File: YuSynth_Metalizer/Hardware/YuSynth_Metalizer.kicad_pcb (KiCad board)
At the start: 2 copper layers, 29 x 108 mm, 83 parts, among them J37 CV1, J38 CV2, J39 In, J40 Out, Q1 BC547, Q10 BC547, Q11 BC557, Q12 BC547, Q2 BC547, Q3 BC547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

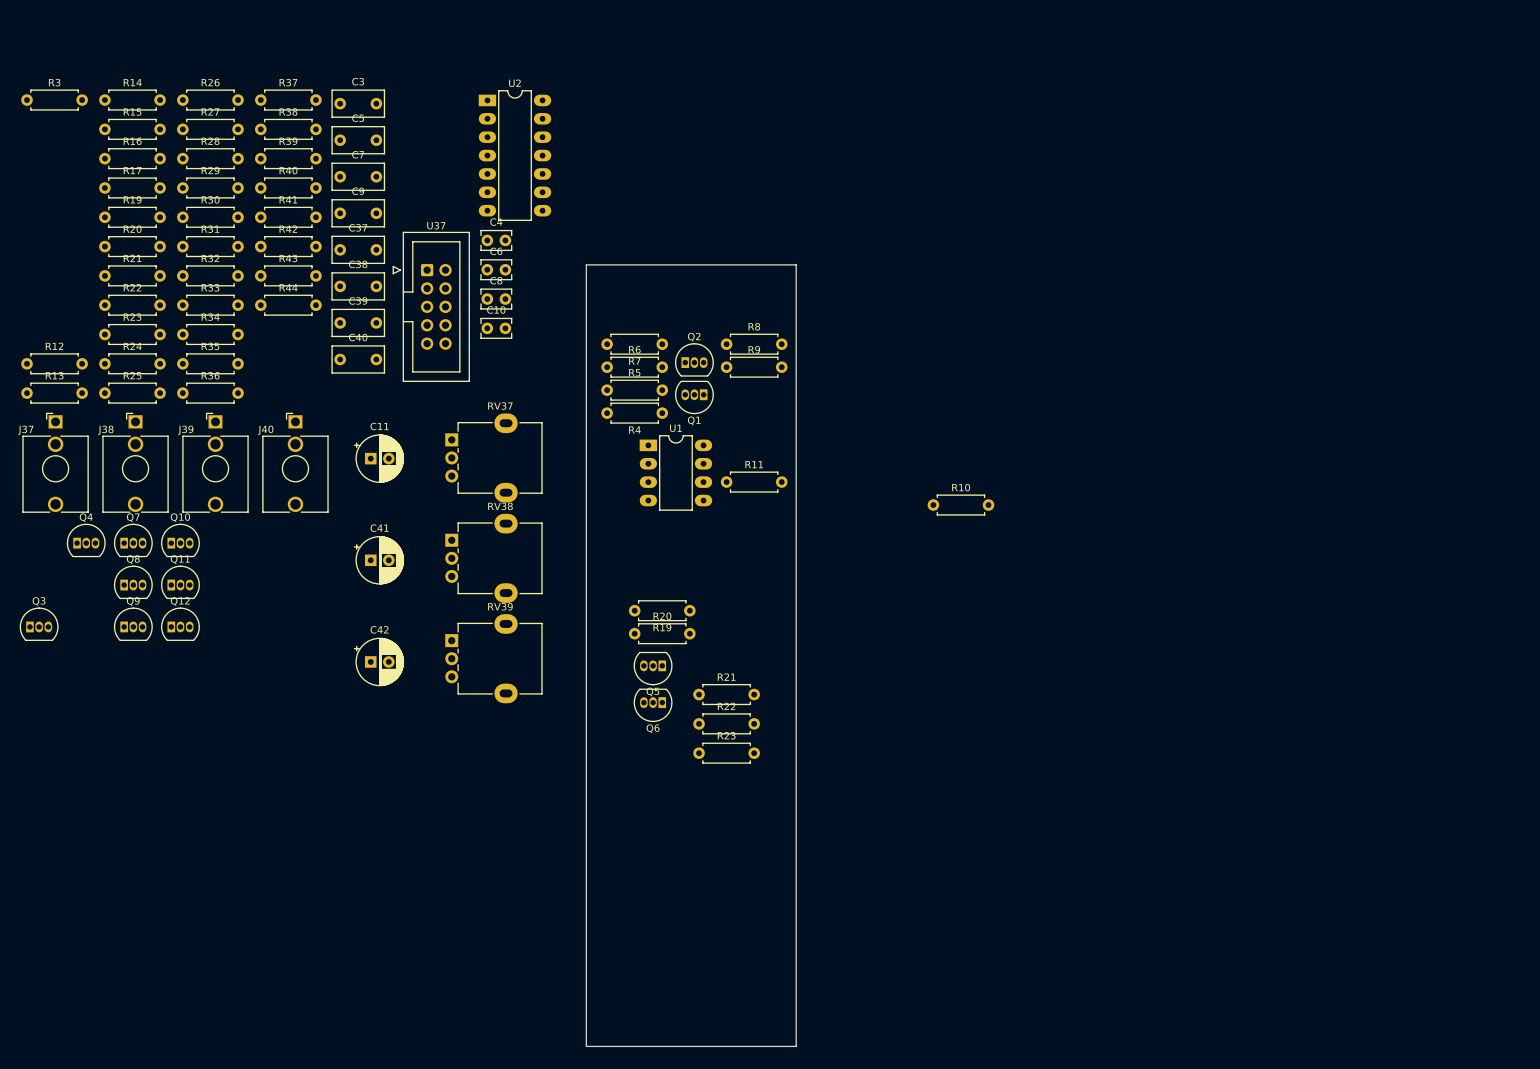
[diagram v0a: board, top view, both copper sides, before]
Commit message: Fixed OpAmp supply range error & redid PCB
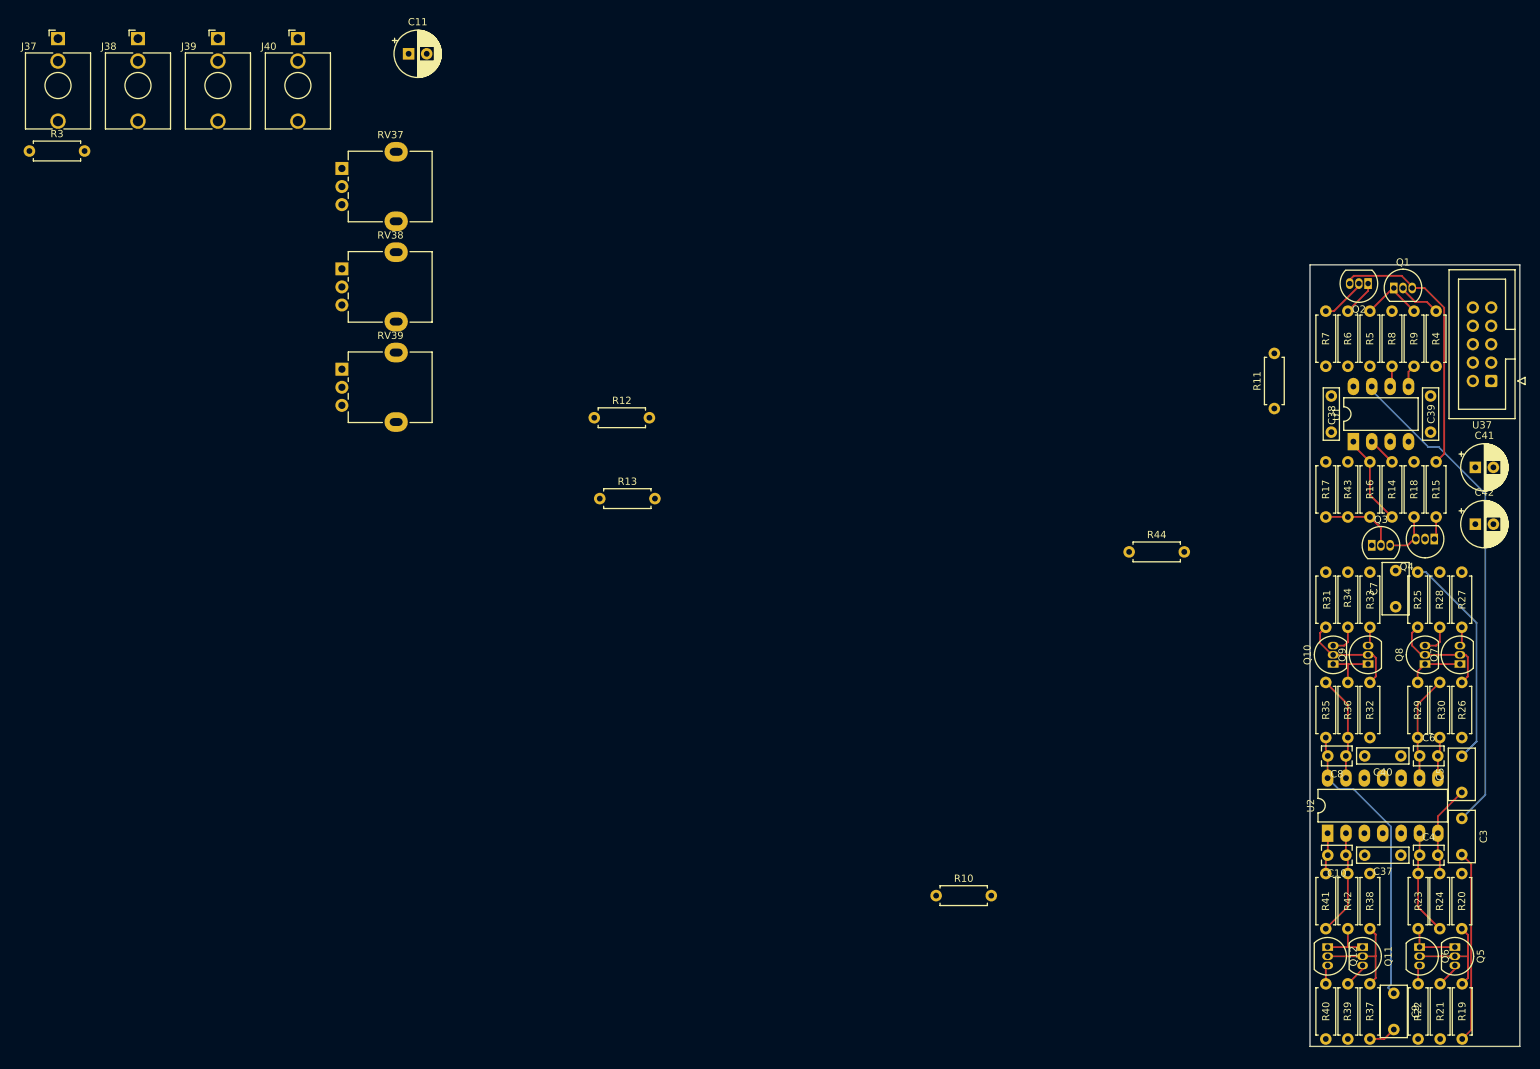
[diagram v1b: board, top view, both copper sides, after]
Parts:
- removed the R19 at (33.5, 43.4)
- removed the R19 at (114.3, 97.8)
- removed the R20 at (33.5, 47.5)
- removed the R20 at (106.7, 101.0)
- removed the R21 at (33.5, 51.5)
- removed the R21 at (115.6, 109.4)
- removed the R22 at (33.5, 55.6)
- removed the R22 at (115.6, 113.4)
- removed the R23 at (115.6, 117.5)
- removed the R23 at (33.5, 59.6)
- added R18: 18k, Resistor_THT:R_Axial_DIN0207_L6.3mm_D2.5mm_P7.62mm_Horizontal, F.Cu at (214.4, 84.8)
- added R19: 27k, Resistor_THT:R_Axial_DIN0207_L6.3mm_D2.5mm_P7.62mm_Horizontal, F.Cu at (221.0, 157.0)
- added R20: 68k, Resistor_THT:R_Axial_DIN0207_L6.3mm_D2.5mm_P7.62mm_Horizontal, F.Cu at (221.0, 141.7)
- added R21: 22k, Resistor_THT:R_Axial_DIN0207_L6.3mm_D2.5mm_P7.62mm_Horizontal, F.Cu at (218.0, 157.0)
- added R22: 22k, Resistor_THT:R_Axial_DIN0207_L6.3mm_D2.5mm_P7.62mm_Horizontal, F.Cu at (214.9, 149.4)
- added R23: 10k, Resistor_THT:R_Axial_DIN0207_L6.3mm_D2.5mm_P7.62mm_Horizontal, F.Cu at (214.9, 141.7)
- C37, C38, C39, C40: footprint Capacitor_THT:C_Rect_L7.0mm_W3.5mm_P5.00mm -> Capacitor_THT:C_Rect_L7.0mm_W2.0mm_P5.00mm
- moved R37 200.8 mm to (208.3, 157.0), turned to 90 degrees
- moved R24 200.3 mm to (217.9, 141.7), turned to 90 degrees
- moved R26 194.2 mm to (221.0, 107.7), turned to -90 degrees
- moved R39 193.3 mm to (205.2, 157.0), turned to 90 degrees
- moved R15 189.6 mm to (217.4, 77.2), turned to -90 degrees
- moved R38 188.9 mm to (208.3, 141.7), turned to 90 degrees
- moved Q4 187.6 mm to (217.2, 87.9), turned to 180 degrees
- moved R27 187.0 mm to (221.0, 92.5), turned to -90 degrees
- moved Q3 185.8 mm to (208.5, 88.8)
- moved R28 185.4 mm to (217.9, 100.1), turned to 90 degrees
- moved Q7 185.4 mm to (220.7, 105.2), turned to 90 degrees
- moved R30 185.2 mm to (217.9, 107.7), turned to -90 degrees
- moved R14 184.8 mm to (211.3, 77.2), turned to -90 degrees
- moved R29 183.8 mm to (214.9, 107.7), turned to -90 degrees
- moved C3 183.8 mm to (221.0, 126.5), turned to -90 degrees
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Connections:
- C37 pad 2: Net-(U2E-V+) -> +12V
- C38 pad 2: Net-(U1C-V+) -> +12V
- C39 pad 1: Net-(U1C-V-) -> -12V
- C40 pad 1: Net-(U2E-V-) -> -12V
- U1 pad 4: Net-(U1C-V-) -> -12V
- U1 pad 8: Net-(U1C-V+) -> +12V
- U2 pad 11: Net-(U2E-V-) -> -12V
- U2 pad 4: Net-(U2E-V+) -> +12V
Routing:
- net Net-(C3-Pad1): track 0.00 -> 68.4 mm
- net Net-(C8-Pad2): track 0.00 -> 40.8 mm
- net Net-(Q1-E): track 0.00 -> 37.5 mm
- net Net-(C5-Pad2): track 0.00 -> 30.3 mm
- net Net-(C3-Pad2): track 0.00 -> 26.5 mm
- net Net-(Q7-B): track 0.00 -> 15.1 mm
- net Net-(Q5-B): track 0.00 -> 15.0 mm
- net Net-(Q11-B): track 0.00 -> 14.9 mm
- net Net-(Q10-B): track 0.00 -> 14.8 mm
- net Net-(U2C--): track 0.00 -> 14.6 mm
- net Net-(U2D--): track 0.00 -> 14.6 mm
- net Net-(U2B--): track 0.00 -> 14.6 mm
- net Net-(U2A--): track 0.00 -> 14.6 mm
- net Net-(C4-Pad2): track 0.00 -> 12.7 mm
- net Net-(R14-Pad2): track 0.00 -> 12.6 mm
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
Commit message: Main board & panel nearly done
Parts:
- removed U37: ~, Connector_IDC:IDC-Header_2x05_P2.54mm_Vertical
- added J41: Conn_01x10, Connector_PinHeader_2.54mm:PinHeader_1x10_P2.54mm_Vertical, B.Cu at (201.9, 51.8)
- added J42: Conn_01x10, Connector_PinHeader_2.54mm:PinHeader_1x10_P2.54mm_Vertical, B.Cu at (201.9, 134.4)
- added J43: Conn_01x10, Connector_PinHeader_2.54mm:PinHeader_1x10_P2.54mm_Vertical, B.Cu at (227.1, 134.4)
- added J44: Conn_01x10, Connector_PinHeader_2.54mm:PinHeader_1x10_P2.54mm_Vertical, B.Cu at (227.1, 51.8)
- added J45: Conn_02x05_Odd_Even, Connector_IDC:IDC-Header_2x05_P2.54mm_Vertical, F.Cu at (219.7, 53.8)
- C41, C42: moved to B.Cu
- moved R7 22.2 mm to (218.4, 71.6)
- moved Q2 21.5 mm to (223.7, 67.2), turned to -90 degrees
- moved C42 21.4 mm to (217.7, 65.1)
- moved C41 19.3 mm to (208.5, 65.1)
- moved R11 18.1 mm to (211.0, 61.3), turned to -90 degrees
- moved Q3 16.8 mm to (223.7, 81.5), turned to -90 degrees
- moved Q1 14.8 mm to (223.7, 61.7), turned to -90 degrees
- moved Q4 6.60 mm to (223.7, 87.1), turned to -90 degrees
- moved C39 6.56 mm to (221.2, 77.9)
- moved R5 5.89 mm to (205.0, 68.9)
- moved R6 5.62 mm to (208.0, 68.9)
- moved R14 5.59 mm to (214.1, 82.1)
- moved R16 5.59 mm to (211.0, 82.1)
- moved R17 5.59 mm to (204.9, 89.7)
- moved R18 5.59 mm to (217.1, 89.7)
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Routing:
- net -12V: track 0.00 -> 187.8 mm, vias 0 -> 1
- net +12V: track 0.00 -> 176.3 mm
- net Net-(C5-Pad2): track 30.3 -> 0.00 mm
- net Net-(C6-Pad2): track 5.72 -> 24.8 mm
- net Net-(Q1-E): track 37.5 -> 20.5 mm
- net Net-(Q2-C): track 4.97 -> 20.9 mm
- net Net-(Q1-C): track 8.98 -> 23.7 mm
- net Net-(C3-Pad1): track 68.4 -> 80.3 mm
- net Net-(C7-Pad2): track 0.00 -> 11.2 mm
- net Net-(Q3-B): track 10.6 -> 21.7 mm
- net Net-(U1B--): track 2.90 -> 12.1 mm
- net Net-(R14-Pad2): track 12.6 -> 4.49 mm
- net Net-(Q3-E): track 6.71 -> 0.00 mm
- net Net-(C10-Pad2): track 5.70 -> 0.00 mm
- net Net-(Q4-C): track 3.26 -> 0.00 mm
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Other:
- board size 29 x 108 mm -> 29 x 109 mm
